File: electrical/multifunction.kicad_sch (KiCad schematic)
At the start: 34 parts

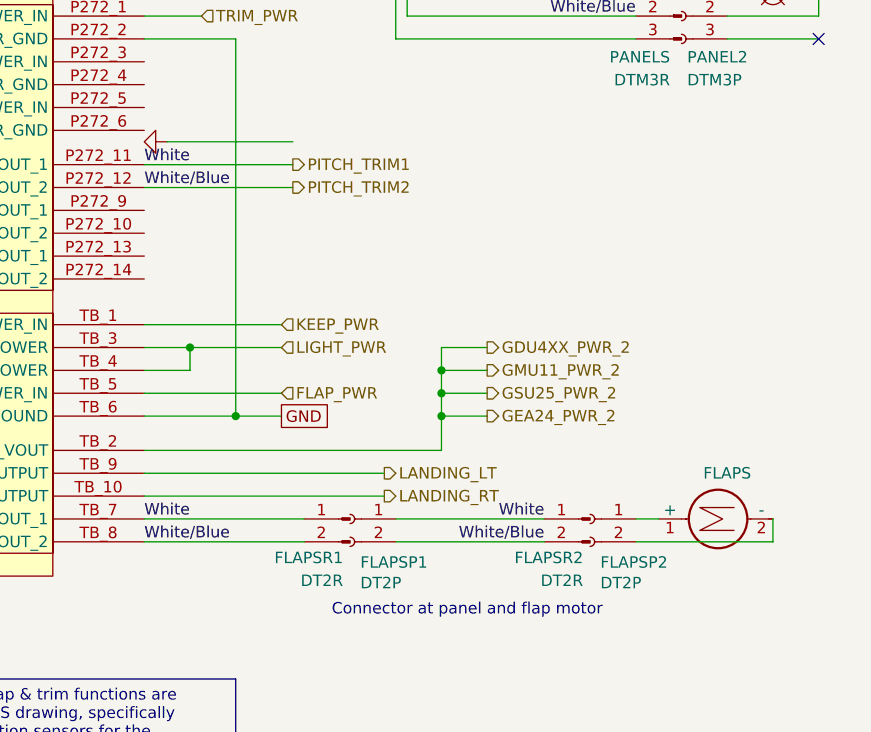
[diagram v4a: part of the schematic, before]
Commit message: Added AWG wires.
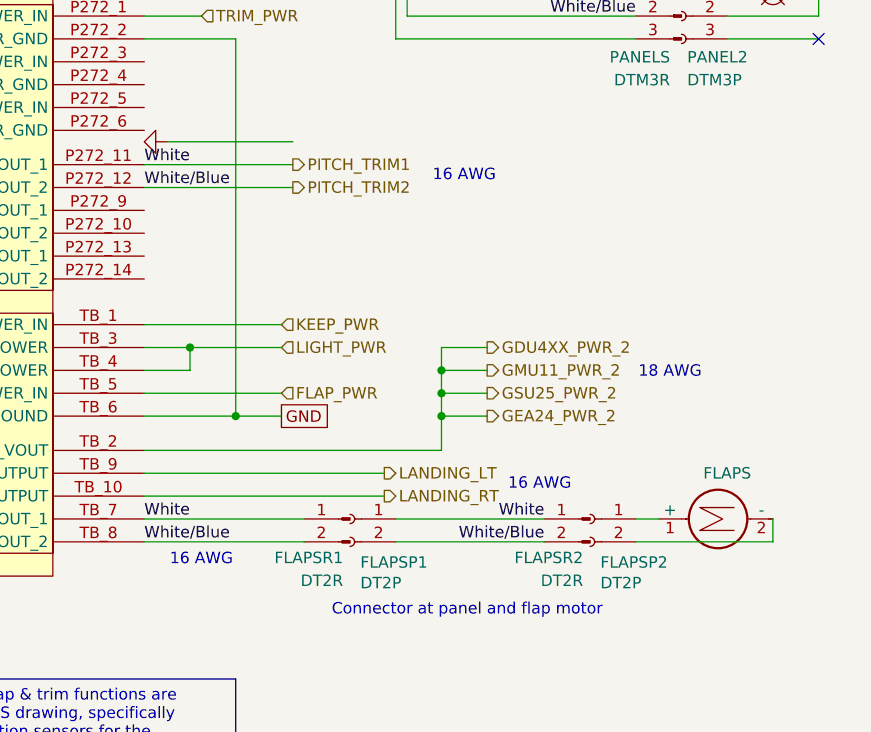
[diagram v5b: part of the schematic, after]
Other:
- note added: "16 AWG"
- note added: "18 AWG"
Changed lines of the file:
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@@
 		(title "Flaps, Lights & Trim")
 		(date "2025-12-24")
-		(rev "1.2")
+		(rev "1.2.1")
 		(company "N877RV")
 	)
@@
 		)
 	)
+	(text "16 AWG"
+		(exclude_from_sim no)
+		(at 125.222 213.36 0)
+		(effects
+			(font
+				(size 1.27 1.27)
+			)
+		)
+	)
 	(text "Connector at panel and flap motor"
 		(exclude_from_sim no)
@@
 			)
 			(justify left)
+		)
+	)
+	(text "18 AWG"
+		(exclude_from_sim no)
+		(at 139.7 200.914 0)
+		(effects
+			(font
+				(size 1.27 1.27)
+			)
 		)
 	)
@@
 		)
 	)
+	(text "16 AWG"
+		(exclude_from_sim no)
+		(at 87.63 221.742 0)
+		(effects
+			(font
+				(size 1.27 1.27)
+			)
+		)
+	)
+	(text "16 AWG"
+		(exclude_from_sim no)
+		(at 116.84 179.07 0)
+		(effects
+			(font
+				(size 1.27 1.27)
+			)
+		)
+	)

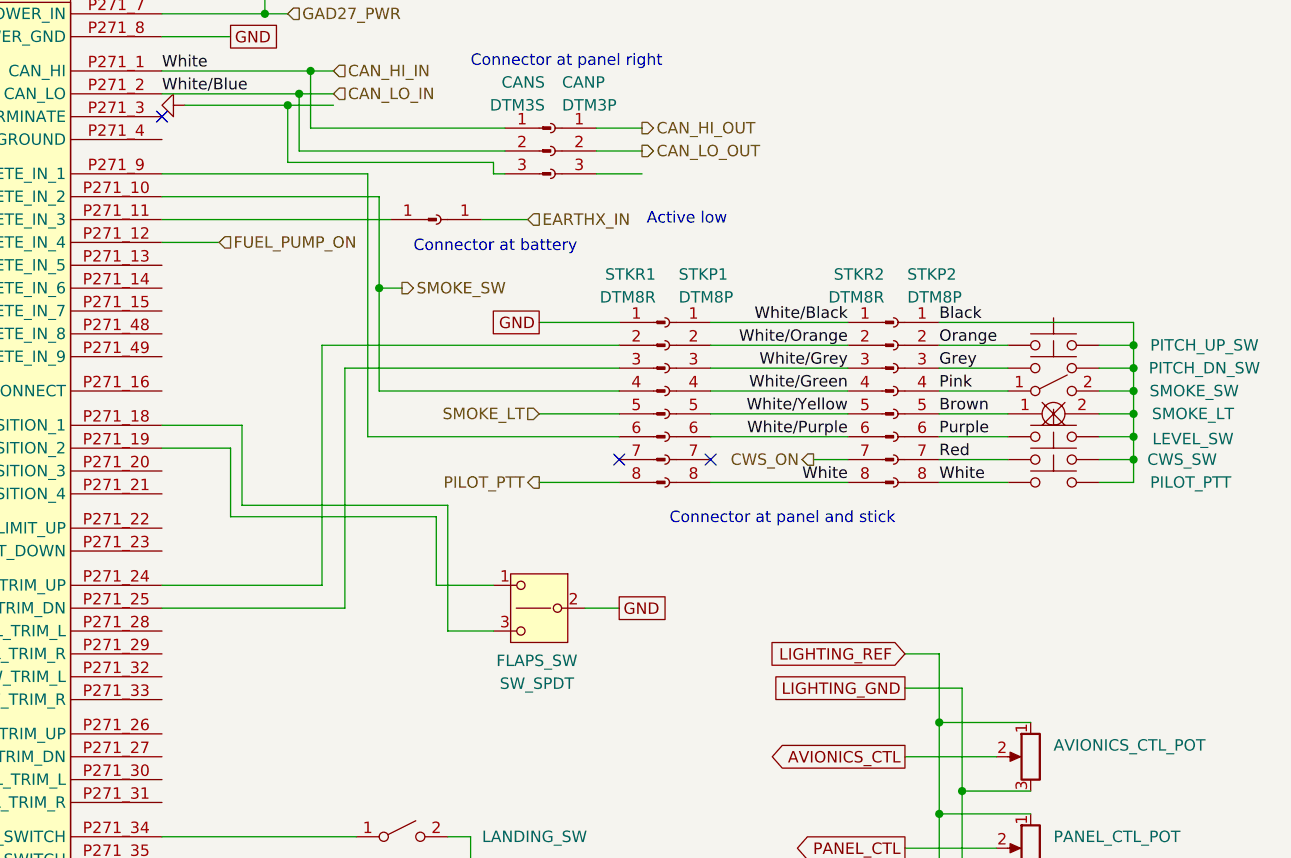
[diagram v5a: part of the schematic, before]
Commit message: Added extra connector for GDL 52, rewired stick to have flaps up/down instead of level/smoke. Put smoke on panel.
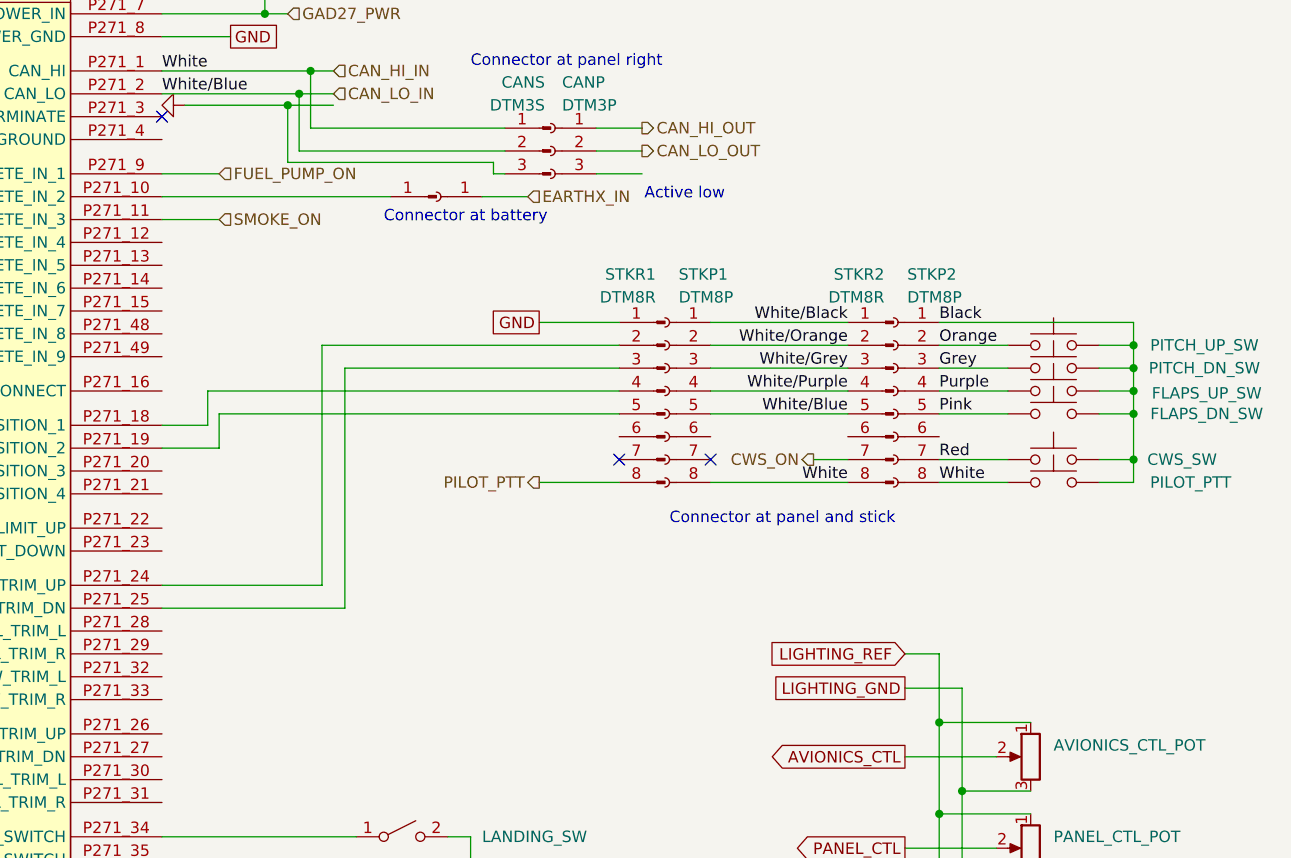
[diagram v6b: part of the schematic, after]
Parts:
- removed FLAPS_SW: SW_SPDT, symbol flyerx:SW_SPDT
- removed SMOKE_LT: ~, symbol flyerx:Bulb
- removed SMOKE_SW: ~, symbol Switch:SW_SPST
- added FLAPS_DN_SW: SW_Push, symbol Switch:SW_Push
- renumbered LEVEL_SW to FLAPS_UP_SW
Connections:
- net Brown is gone; now on net Pink: STKP2.5 (Pin_5)
- net SMOKE_LT is gone; now on an unnamed net: STKR1.5 (Pin_5)
- net White/Green is gone; now on net White/Purple: STKP1.4 (Pin_4), STKR2.4 (Pin_4)
- net White/Yellow is gone; now on net CAN_LO_IN: STKP1.5 (Pin_5), STKR2.5 (Pin_5)
- net Black: now also FLAPS_DN_SW.2
- net FUEL_PUMP_ON: now also GAD27.P271_9 (DISCRETE_IN_1); no longer GAD27.P271_12 (DISCRETE_IN_4)
- net Pink: now also FLAPS_DN_SW.1; no longer STKP2.4 (Pin_4)
- net Purple: now also STKP2.4 (Pin_4); no longer STKP2.6 (Pin_6)
- net White/Purple: no longer STKP1.6 (Pin_6), STKR2.6 (Pin_6)
- net at EARTHXP.1 (Pin_1): now also GAD27.P271_10 (DISCRETE_IN_2); no longer GAD27.P271_11 (DISCRETE_IN_3)
- net at GAD27.P271_18 (FLAP_UP_1_SWITCH/ABS_FLAP_POSITION_1): now also STKR1.4 (Pin_4)
- net at STKR1.6 (Pin_6): no longer GAD27.P271_9 (DISCRETE_IN_1)
- removed net SMOKE_SW: GAD27.P271_10 (DISCRETE_IN_2), STKR1.4 (Pin_4)
- new net SMOKE_ON: GAD27.P271_11 (DISCRETE_IN_3)
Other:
- moved on the sheet: FLAPS_UP_SW

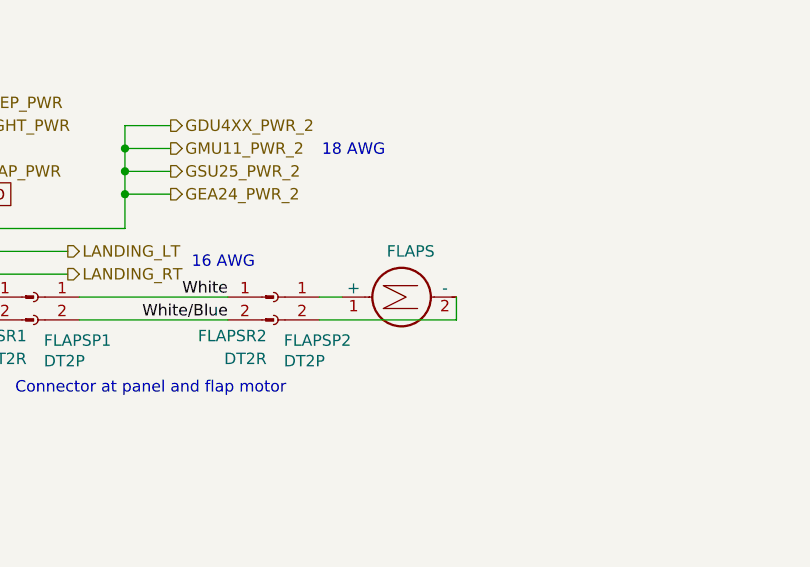
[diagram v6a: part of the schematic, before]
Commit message: Added beacon and added colors for flaps
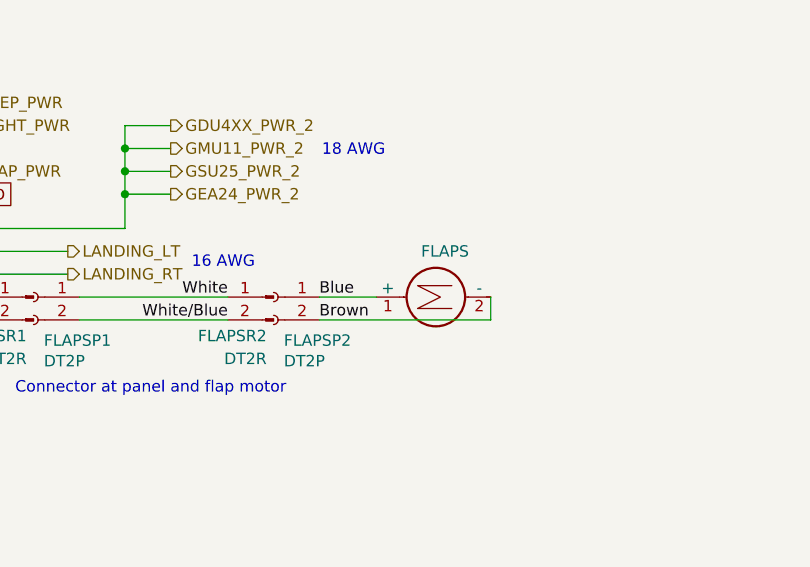
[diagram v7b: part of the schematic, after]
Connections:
- net Blue: now reaches FLAPS.1 (+), FLAPSP2.1 (Pin_1)
- net Brown: now reaches FLAPS.2 (-), FLAPSP2.2 (Pin_2)
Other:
- moved on the sheet: FLAPS
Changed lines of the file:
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@@
 	(title_block
 		(title "Flaps, Lights & Trim")
-		(date "2025-12-31")
-		(rev "1.2.2")
+		(date "2026-01-01")
+		(rev "1.2.3")
 		(company "N877RV")
 	)
@@
 	(wire
 		(pts
-			(xy 135.89 217.17) (xy 138.43 217.17)
-		)
-		(stroke
-			(width 0)
-			(type default)
-		)
-	)
-	(wire
-		(pts
 			(xy 142.24 66.04) (xy 157.48 66.04)
 		)
@@
 	(wire
 		(pts
-			(xy 135.89 219.71) (xy 151.13 219.71)
+			(xy 135.89 219.71) (xy 154.94 219.71)
 		)
 		(stroke
@@
 	(wire
 		(pts
+			(xy 135.89 217.17) (xy 142.24 217.17)
+		)
+		(stroke
+			(width 0)
+			(type default)
+		)
+	)
+	(wire
+		(pts
 			(xy 167.64 78.74) (xy 175.26 78.74)
 		)
@@
 	(wire
 		(pts
-			(xy 151.13 217.17) (xy 151.13 219.71)
+			(xy 154.94 217.17) (xy 154.94 219.71)
 		)
 		(stroke
@@
 		)
 	)
+	(label "Blue"
+		(at 135.89 217.17 0)
+		(effects
+			(font
+				(size 1.27 1.27)
+			)
+			(justify left bottom)
+		)
+	)
 	(label "White"
 		(at 135.89 158.75 180)
@@
 			)
 			(justify right bottom)
+		)
+	)
+	(label "Brown"
+		(at 135.89 219.71 0)
+		(effects
+			(font
+				(size 1.27 1.27)
+			)
+			(justify left bottom)
 		)
 	)
@@
 	(symbol
 		(lib_id "Motor:Motor_DC")
-		(at 143.51 217.17 90)
+		(at 147.32 217.17 90)
 		(unit 1)
 		(exclude_from_sim no)
@@
 		(fields_autoplaced yes)
 		(property "Reference" "FLAPS"
-			(at 146.05 212.09 90)
+			(at 149.86 212.09 90)
 			(effects
 				(font
@@
 		)
 		(property "Value" "Motor_DC"
-			(at 147.32 212.09 0)
+			(at 151.13 212.09 0)
 			(effects
 				(font
@@
 		)
 		(property "Footprint" ""
-			(at 145.796 217.17 0)
+			(at 149.606 217.17 0)
 			(effects
 				(font
@@
 		)
 		(property "Datasheet" "~"
-			(at 145.796 217.17 0)
+			(at 149.606 217.17 0)
 			(effects
 				(font
@@
 		)
 		(property "Description" ""
-			(at 143.51 217.17 0)
-			(effects
-				(font
+			(at 147.32 217.17 0)
+			(effects
+				(font
